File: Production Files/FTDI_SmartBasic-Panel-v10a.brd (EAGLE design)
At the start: 170.7 x 117.3 mm, 563 parts, among them U1 FT232RLSSOP, U10 TS3USB221A, U11 FT232RLSSOP, U12 MIC5219 3.3V, U13 TS3USB221A, U14 FT232RLSSOP, U15 MIC5219 3.3V, U16 TS3USB221A, U17 FT232RLSSOP, U18 MIC5219 3.3V, U19 TS3USB221A, U2 MIC5219 3.3V, U20 FT232RLSSOP, U21 MIC5219 3.3V, U22 TS3USB221A, U23 FT232RLSSOP, U24 MIC5219 3.3V, U25 TS3USB221A, U26 FT232RLSSOP, U27 MIC5219 3.3V, U28 TS3USB221A, U29 FT232RLSSOP, U3 TS3USB221A, U30 MIC5219 3.3V, U31 TS3USB221A, U32 FT232RLSSOP, U33 MIC5219 3.3V, U34 TS3USB221A, U35 FT232RLSSOP, U36 MIC5219 3.3V, U37 TS3USB221A, U38 FT232RLSSOP, U39 MIC5219 3.3V, U4 TS3USB221A, U40 TS3USB221A, U41 FT232RLSSOP, U42 MIC5219 3.3V, U43 TS3USB221A, U44 FT232RLSSOP, U45 MIC5219 3.3V, U46 TS3USB221A, U47 FT232RLSSOP, U48 MIC5219 3.3V, U49 TS3USB221A, U5 FT232RLSSOP, U50 FT232RLSSOP, U51 MIC5219 3.3V, U52 TS3USB221A, U53 FT232RLSSOP, U54 MIC5219 3.3V, U55 TS3USB221A, U56 FT232RLSSOP, U57 MIC5219 3.3V, U58 TS3USB221A, U59 FT232RLSSOP, U6 MIC5219 3.3V, U60 MIC5219 3.3V, U7 TS3USB221A, U8 FT232RLSSOP, U9 MIC5219 3.3V

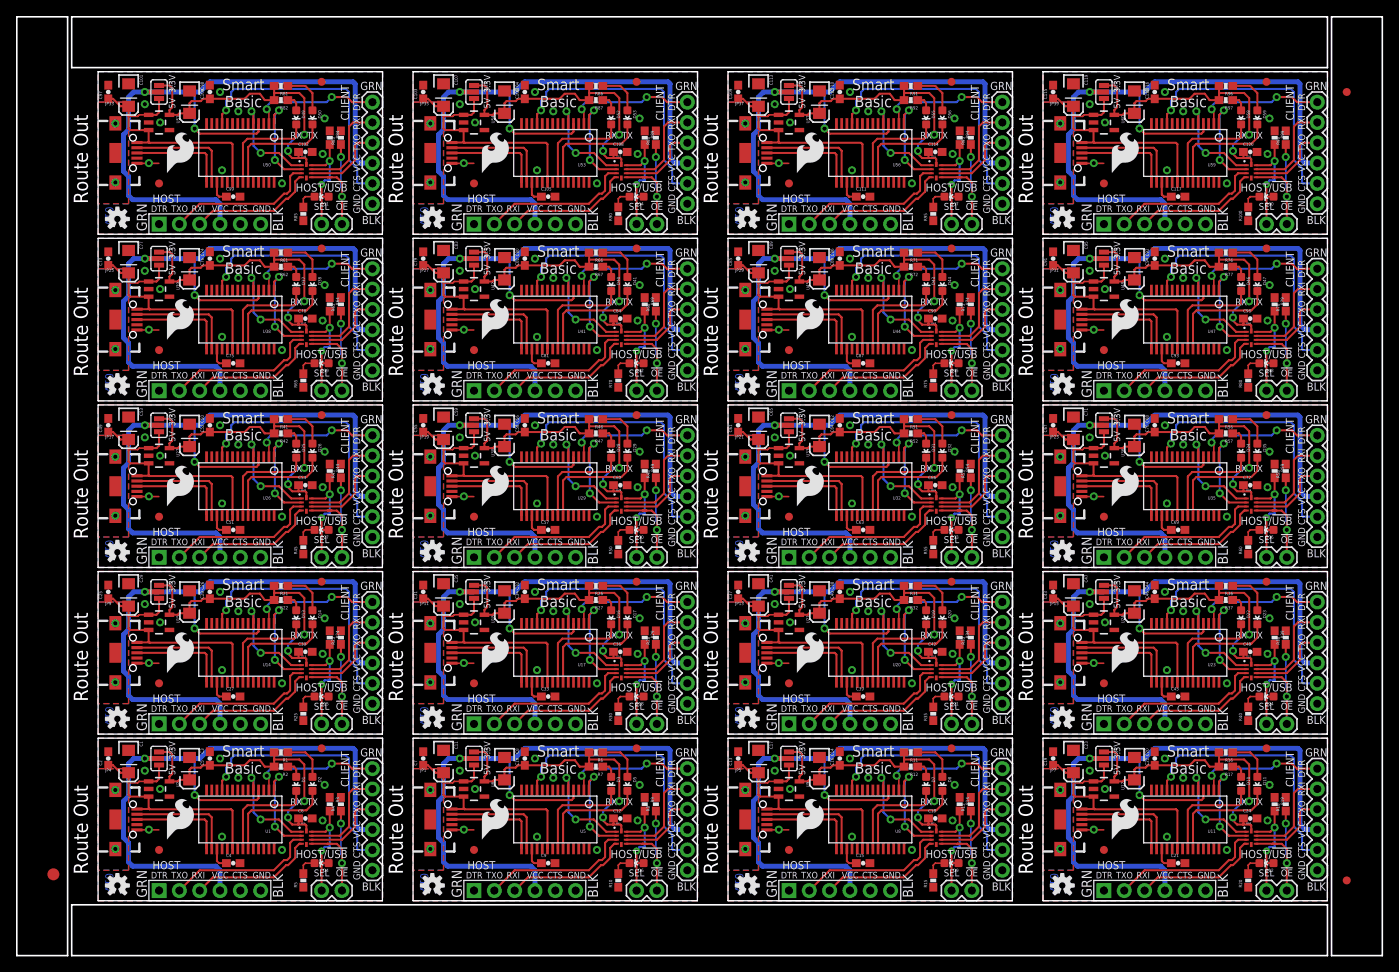
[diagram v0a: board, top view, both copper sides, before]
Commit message: re-created panel with correct silk
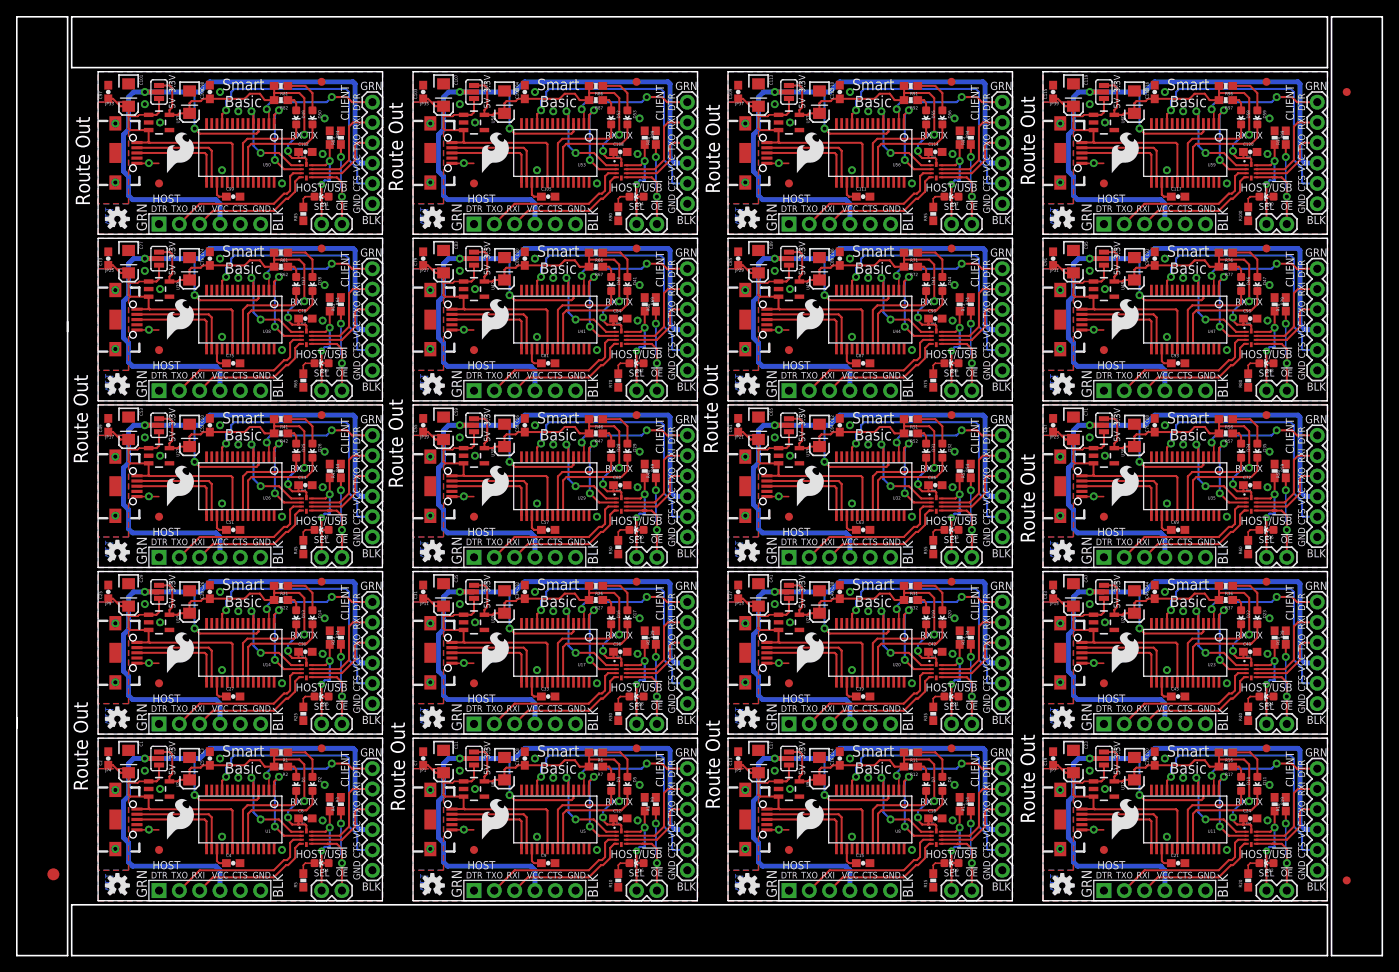
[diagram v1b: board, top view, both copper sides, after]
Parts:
- removed E$6: (no value), SparkFun-Aesthetics:FIDUCIAL-1X2
- added E$7: (no value), SparkFun-Aesthetics:FIDUCIAL-1X2
- moved E$5 98.6 mm to (166.2, 9.40), turned to 0 degrees
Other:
- outline, holes or cut-outs redrawn
- board text added: "v11"
- board text removed: "v10"
